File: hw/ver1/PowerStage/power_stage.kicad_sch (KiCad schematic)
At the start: 56 parts, among them J4 Conn_02x12_Odd_Even, J5 Conn_01x02_Socket, Q1 2N7002, SW1 SW_DIP_x03, U3 74HC4051, U4 LTC7871

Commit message: Save this morning's effort
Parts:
- added C23, C28, C29, C30, C31, C32, C33, C34, C35, C36, C37, C38, C39, C40: 2uF, symbol Device:C
- added C24, C25, C26, C27: 220uF, symbol Device:C_Polarized
- added R35, R52: 10k, Resistor_SMD:R_0603_1608Metric, symbol Device:R_US
- added U10: LM1117MP-3.3, Package_TO_SOT_SMD:SOT-223-3_TabPin2, symbol Regulator_Linear:LM1117MP-3.3
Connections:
- net +12P: now also C40.1, U10.3 (VI)
- net +3.3VP: now also C39.1, U10.2 (VO)
- net +5P: now also R35.2
- net GND: now also C23.2, C24.2, C25.2, C26.2, C27.2, C28.2, C29.2, C30.2, C31.2, C32.2, C33.2, C34.2, C35.2, C36.2, C37.2, C38.2, C39.2, C40.2, U10.1 (GND)
- net GNDD: now also R52.2
- net HT: now also C31.1, C32.1, C33.1, C34.1, C35.1, C36.1, C37.1, C38.1
- net VBUS: no longer R25.1
- net Phase1/SNSA+: now reaches U4.17 (SNSA1+)
- net Phase1/SNSD-: now reaches U4.18 (SNS1-)
- net Phase1/SNSD+: now reaches U4.19 (SNSD1+)
- net Phase2/SNSD+: now reaches U4.20 (SNSD2+)
- net Phase2/SNSD-: now reaches U4.21 (SNS2-)
- net Phase2/SNSA+: now reaches U4.22 (SNSA2+)
- net Phase3/SNSA+: now reaches U4.23 (SNSA3+)
- net Phase3/SNSD-: now reaches U4.24 (SNS3-)
- net Phase3/SNSD+: now reaches U4.25 (SNSD3+)
- net Phase1/PWMEN: now reaches U4.28 (PWMEN)
- net Phase1/PWMEN: now also R35.1
- net Phase1/PWM: now reaches U4.29 (PWM1)
- net Phase2/PWM: now reaches U4.31 (PWM2)
- net Phase3/PWM: now reaches U4.32 (PWM3)
- net Phase4/PWM: now reaches U4.33 (PWM4)
- net DisabledPhase5/PWM: now reaches U4.34 (PWM5)
- net DisabledPhase6/PWM: now reaches U4.36 (PWM6)
- net at U4.50 (CLKOUT): now also R52.1
- net Phase4/SNSD+: now reaches U4.56 (SNSD4+)
- net Phase4/SNSD-: now reaches U4.57 (SNS4-)
- net Phase4/SNSA+: now reaches U4.58 (SNSA4+)
- net DisabledPhase5/SNSA+: now reaches U4.59 (SNSA5+)
- net DisabledPhase5/SNSD-: now reaches U4.60 (SNS5-)
- net DisabledPhase5/SNSD+: now reaches U4.61 (SNSD5+)
- net DisabledPhase6/SNSD+: now reaches U4.62 (SNSD6+)
- net DisabledPhase6/SNSD-: now reaches U4.63 (SNS6-)
- net DisabledPhase6/SNSA+: now reaches U4.64 (SNSA6+)
- new net VLOW: C23.1, C24.1, C25.1, C26.1, C27.1, C28.1, C29.1, C30.1, R25.1
- no-connect marks 2 -> 1
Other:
- added sheet DisabledPhase5 (power_stage_n_disabled.kicad_sch)
- added sheet DisabledPhase6 (power_stage_n_disabled.kicad_sch)
- added sheet Phase1 (power_stage_n.kicad_sch)
- added sheet Phase2 (power_stage_n.kicad_sch)
- added sheet Phase3 (power_stage_n.kicad_sch)
- added sheet Phase4 (power_stage_n.kicad_sch)
- note added: "Input Filtering"
- note added: "Output Filtering"
- moved on the sheet: R25, R26, R3, R4, R5, R6

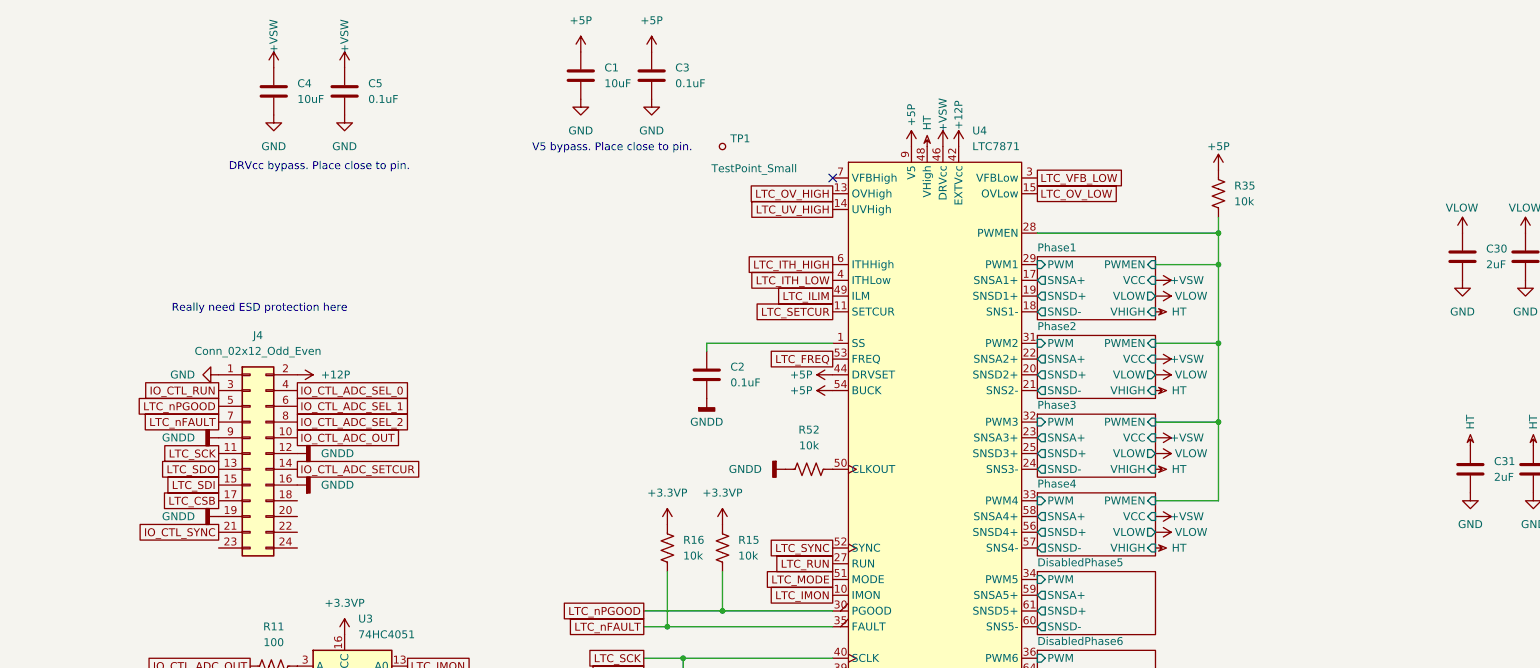
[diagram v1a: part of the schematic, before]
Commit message: Split controller from the power stage. Get a better high level system flow.
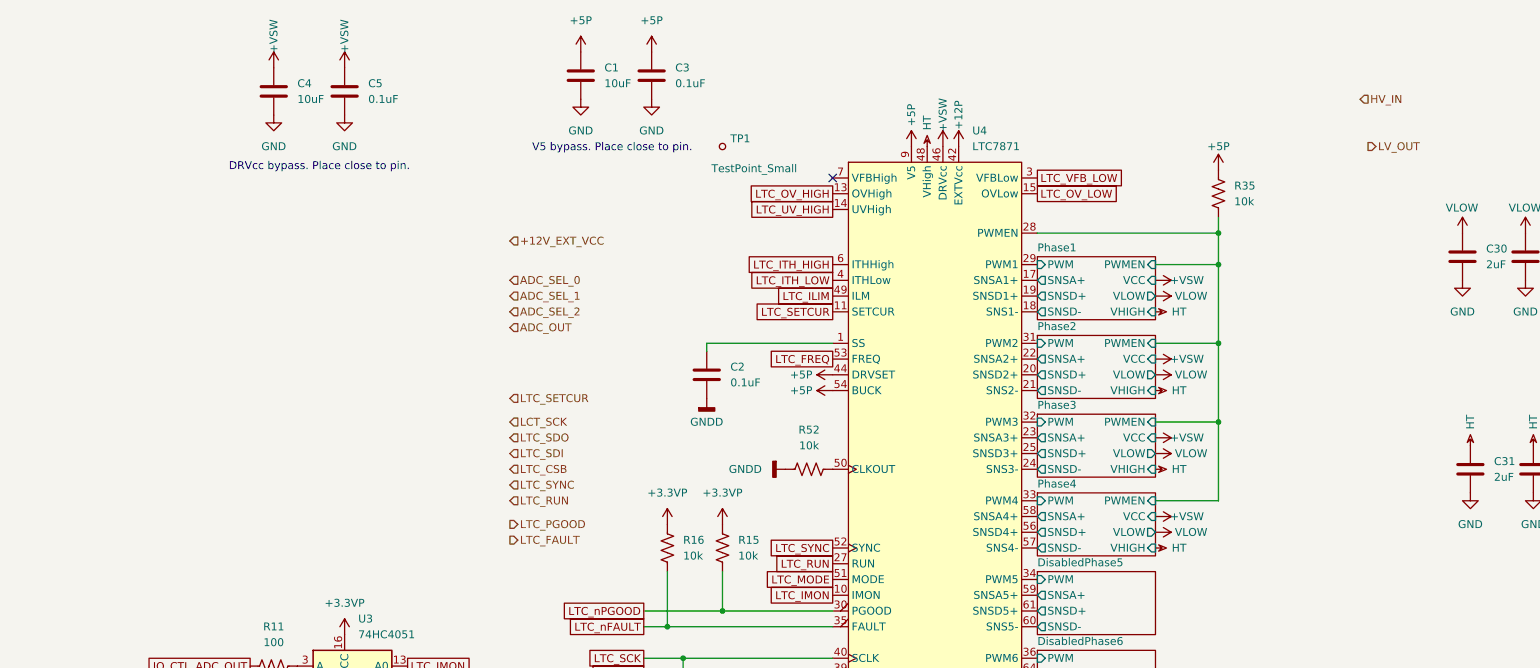
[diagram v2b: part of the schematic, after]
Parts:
- removed J4: Conn_02x12_Odd_Even, symbol Connector_Generic:Conn_02x12_Odd_Even
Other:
- note removed: "Really need ESD protection here"

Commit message: Sync wip
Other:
- note added: "Only enable one at a time. Both GND == floating. NPN PNP? Or MOS?"

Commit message: Save lunchtime work
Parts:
- removed JP2: Jumper_3_Open, Jumper:SolderJumper-3_P1.3mm_Open_RoundedPad1.0x1.5mm_NumberLabels, symbol Jumper:Jumper_3_Open
- removed JP4: Jumper_2_Open, symbol Jumper:Jumper_2_Open
- removed Q1: 2N7002, Package_TO_SOT_SMD:SOT-23, symbol Transistor_FET:2N7002
- added C65: 2uF, symbol Device:C
- added JP3: SolderJumper_2_Bridged, Jumper:SolderJumper-2_P1.3mm_Bridged_RoundedPad1.0x1.5mm, symbol Jumper:SolderJumper_2_Bridged
- added Q1: BSS84, Package_TO_SOT_SMD:SOT-23, symbol Transistor_FET:BSS84
- added Q6, Q7, Q8: BSS138, Package_TO_SOT_SMD:SOT-23, symbol Transistor_FET:BSS138
- added R61, R65: 100, Resistor_SMD:R_0603_1608Metric, symbol Device:R_US
- added R62, R63, R64, R66: 10k, Resistor_SMD:R_0603_1608Metric, symbol Device:R_US
- R27: value 10k -> 22k
- R28: value 10k -> 1k
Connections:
- net +5P: now also Q1.2 (S), R63.2
- net GND: now also C65.2
- net GNDD: now also Q6.2 (S), Q7.2 (S), Q8.2 (S), R62.1, R66.1
- net LTC_MODE: now also Q6.3 (D), R64.2
- net LTC_SETCUR: now also C65.1
- net LTC_SYNC: now also JP3.2 (B)
- net at R7.2, R9.1: now also Q7.1 (G)
- net at R8.1: now also JP3.1 (A), Q7.3 (D)
- net DisabledPhase5/PWM renamed Phase5/PWM
- net DisabledPhase5/SNSA+ renamed Phase5/SNSA+
- net DisabledPhase5/SNSD+ renamed Phase5/SNSD+
- net DisabledPhase5/SNSD- renamed Phase5/SNSD-
- net DisabledPhase6/PWM renamed Phase6/PWM
- net DisabledPhase6/SNSA+ renamed Phase6/SNSA+
- net DisabledPhase6/SNSD+ renamed Phase6/SNSD+
- net DisabledPhase6/SNSD- renamed Phase6/SNSD-
- net IO_CTL_ADC_OUT renamed IO_ADC_OUT
- net IO_CTL_ADC_SEL_0 renamed IO_ADC_SEL_0
- net IO_CTL_ADC_SEL_1 renamed IO_ADC_SEL_1
- net IO_CTL_ADC_SEL_2 renamed IO_ADC_SEL_2
- net IO_CTL_ADC_SETCUR renamed IO_LTC_SETCUR
- net IO_CTL_RUN renamed IO_LTC_RUN
- net IO_CTL_SYNC renamed IO_LTC_SYNC
- net LTC_CSB renamed IO_LTC_CSB
- net LTC_SCK renamed IO_LCT_SCK
- net LTC_SDI renamed IO_LTC_SDI
- net LTC_SDO renamed IO_LTC_SDO
- net LTC_nFAULT renamed IO_LTC_FAULT
- net LTC_nPGOOD renamed IO_LTC_PGOOD
- new net: Q6.1 (G), R61.1, R62.2
- new net: Q8.1 (G), R65.1, R66.2
- new net: Q1.1 (G), Q8.3 (D), R63.1
- new net: Q1.3 (D), R64.1
- new net IO_LTC_CCM: R61.2
- new net IO_LTC_DCCM: R65.2
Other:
- removed sheet DisabledPhase5
- removed sheet DisabledPhase6
- added sheet Phase5 (power_stage_n.kicad_sch)
- added sheet Phase6 (power_stage_n.kicad_sch)
- note added: "CCM=0, DCM=0: Burst Mode CCM=0, DCM=1: Discontinuous Conduction Mode CCM=1, DCM=0: Forced Continuous Conduction Mode CCM=1, DCM=1: Forced Continuous Conduction Mode"
- note added: "TODO: This isn't designed yet!"
- note removed: "+5V == Discontinuous Mode GND == Forced Continuous Mode FLT == Burst Mode"
- note removed: "From ltc7871.ipynb, 1kW, 4phase output DCR Sense 30mV"
- note removed: "Only enable one at a time. Both GND == floating. NPN PNP? Or MOS?"
- moved on the sheet: R24

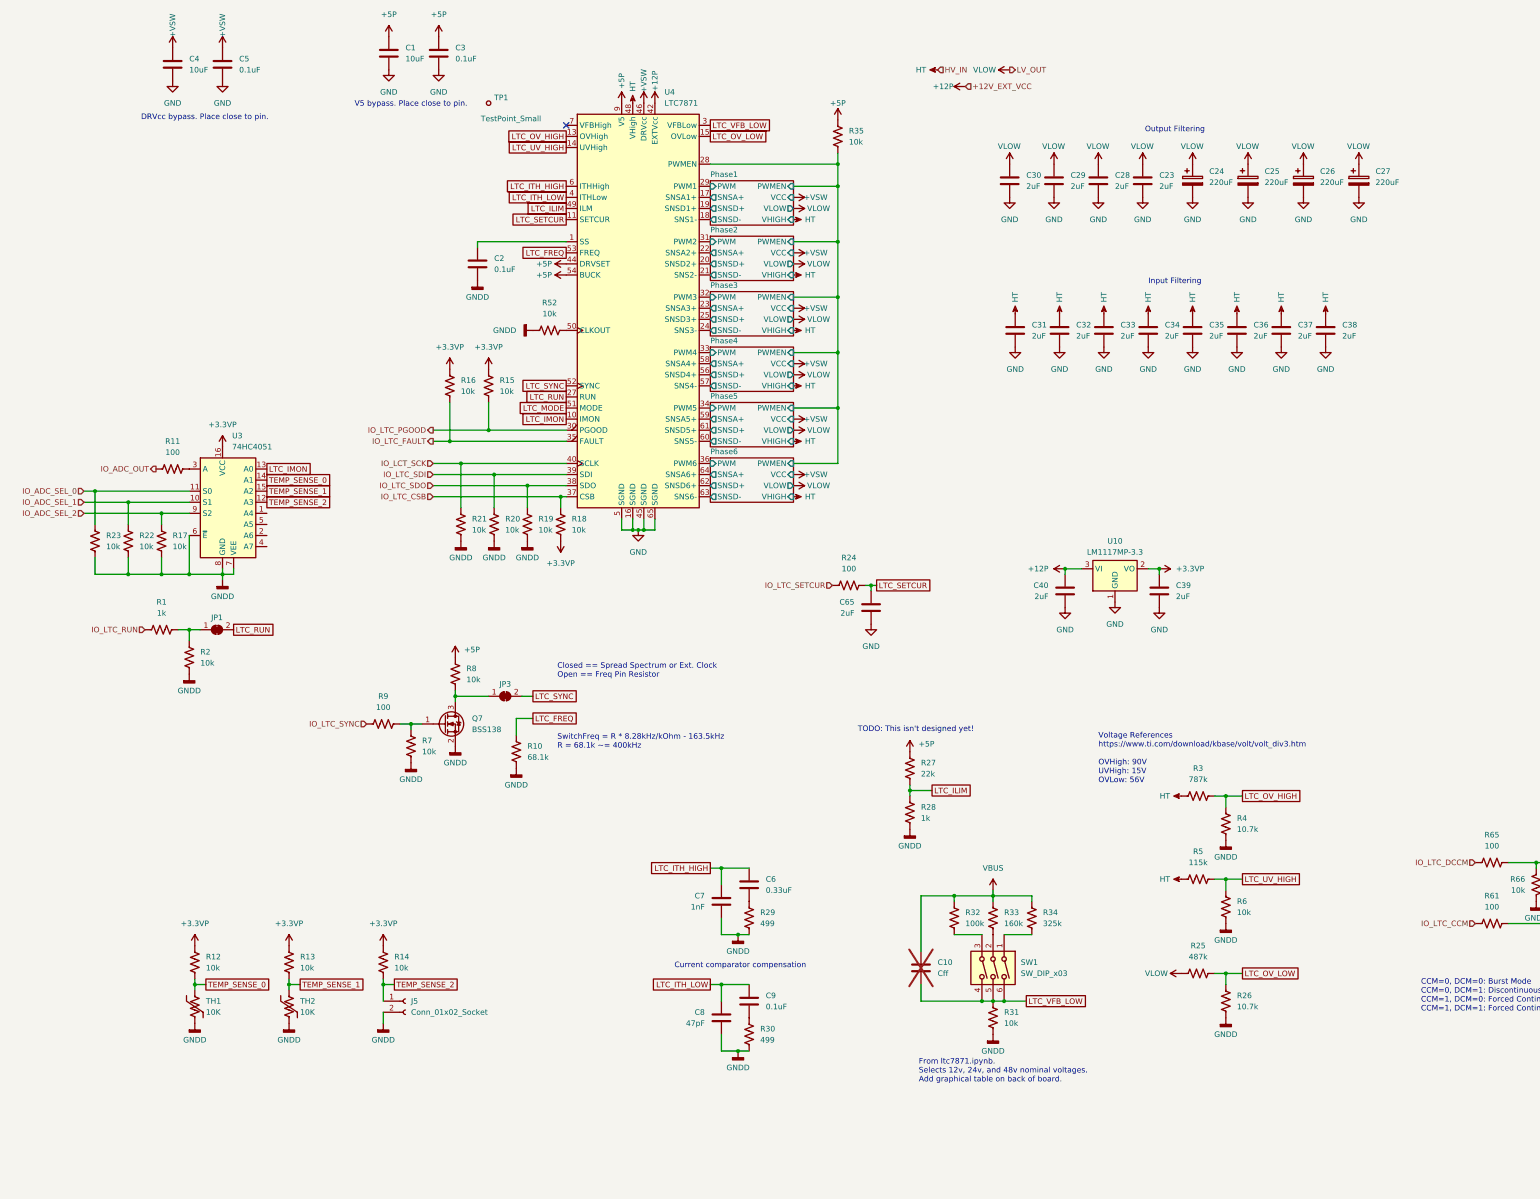
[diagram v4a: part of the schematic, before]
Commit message: Add component part numbers for ordering. Resolve footprints.
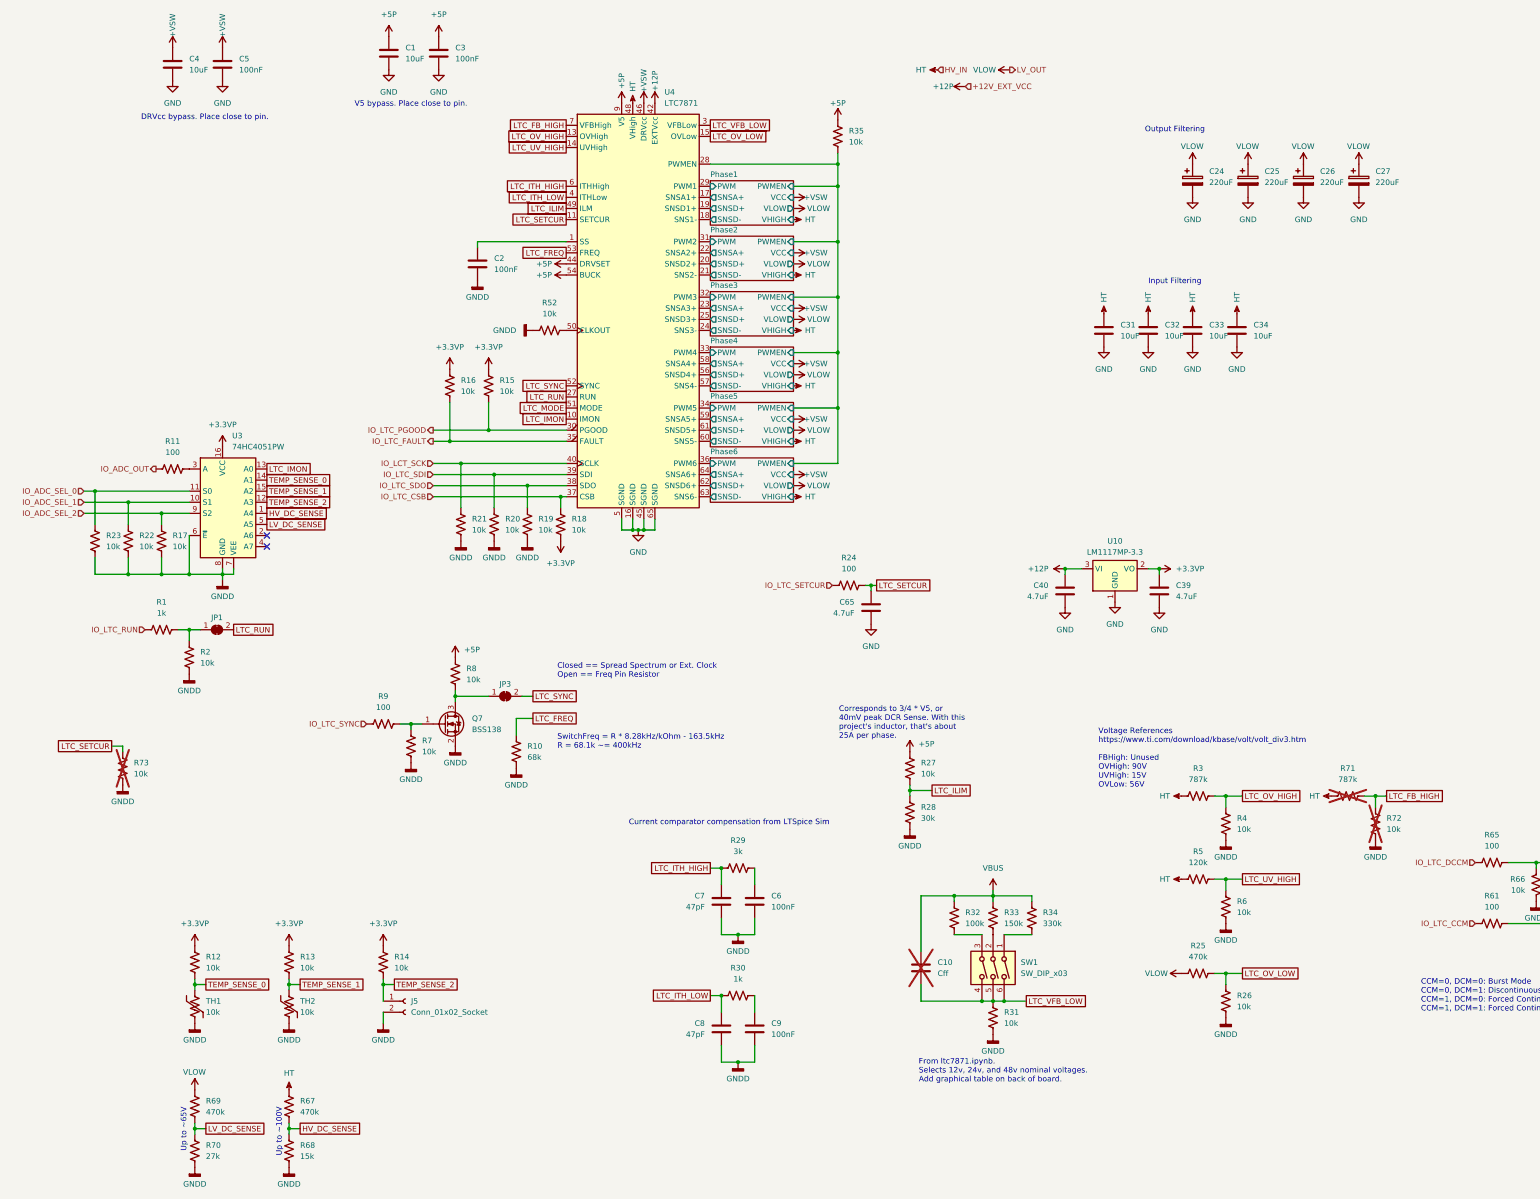
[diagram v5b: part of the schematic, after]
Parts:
- removed C23, C28, C29, C30, C35, C36, C37, C38: 2uF, symbol Device:C
- removed TP1: TestPoint_Small, symbol Connector:TestPoint_Small
- added R67, R69: 470k, Resistor_SMD:R_0603_1608Metric, symbol Device:R_US
- added R68: 15k, Resistor_SMD:R_0603_1608Metric, symbol Device:R_US
- added R70: 27k, Resistor_SMD:R_0603_1608Metric, symbol Device:R_US
- added R71: 787k, Resistor_SMD:R_0603_1608Metric_Pad0.98x0.95mm_HandSolder, symbol Device:R_US
- added R72, R73: 10k, Resistor_SMD:R_0603_1608Metric, symbol Device:R_US
- C1, C4: footprint (none) -> Capacitor_SMD:C_0603_1608Metric; Digikey (none) -> N/A; LCSC (none) -> C96446
- C10: footprint (none) -> Capacitor_SMD:C_0603_1608Metric_Pad1.08x0.95mm_HandSolder; Digikey (none) -> N/A; LCSC (none) -> N/A
- C2, C3, C5, C9: value 0.1uF -> 100nF; footprint (none) -> Capacitor_SMD:C_0603_1608Metric; Digikey (none) -> N/A; LCSC (none) -> C14663
- C24, C25, C26, C27: footprint (none) -> Capacitor_THT:CP_Radial_D10.0mm_P5.00mm; Digikey (none) -> 1189-3789-1-ND; LCSC (none) -> N/A
- C31, C32, C33, C34: value 2uF -> 10uF; footprint (none) -> Capacitor_SMD:C_1210_3225Metric_Pad1.33x2.70mm_HandSolder; Digikey (none) -> 490-16266-1-ND
- C39, C40, C65: value 2uF -> 4.7uF; footprint (none) -> Capacitor_SMD:C_0603_1608Metric; Digikey (none) -> N/A; LCSC (none) -> C19666
- C6: value 0.33uF -> 100nF; footprint (none) -> Capacitor_SMD:C_0603_1608Metric; Digikey (none) -> N/A; LCSC (none) -> C14663
- C7: value 1nF -> 47pF; footprint (none) -> Capacitor_SMD:C_0603_1608Metric; Digikey (none) -> N/A; LCSC (none) -> C1671
- C8: footprint (none) -> Capacitor_SMD:C_0603_1608Metric; Digikey (none) -> N/A; LCSC (none) -> C1671
- J5: footprint (none) -> Connector_PinSocket_2.54mm:PinSocket_1x02_P2.54mm_Vertical; Digikey (none) -> N/A; LCSC (none) -> N/A
- JP1, JP3: Digikey (none) -> N/A; LCSC (none) -> N/A
- Q1: Digikey (none) -> 5272-BSS84CT-ND; LCSC (none) -> N/A
- Q6, Q7, Q8: Digikey (none) -> 5272-BSS138CT-ND; LCSC (none) -> N/A
- R1: Digikey (none) -> N/A; LCSC (none) -> C21190
- R10: value 68.1k -> 68k; Digikey (none) -> N/A; LCSC (none) -> C23231
- R11, R24, R61, R65, R9: Digikey (none) -> N/A; LCSC (none) -> C22775
- R12, R13, R14, R15, R16, R17, R18, R19, R2, R20, R21, R22, R23, R31, R35, R52, R6, R62, R63, R64, R66, R7, R8: Digikey (none) -> N/A; LCSC (none) -> C25804
- R25: value 487k -> 470k; Digikey (none) -> N/A; LCSC (none) -> C23178
- R26, R4: value 10.7k -> 10k; Digikey (none) -> N/A; LCSC (none) -> C25804
- R27: value 22k -> 10k; Digikey (none) -> N/A; LCSC (none) -> C25804
- R28: value 1k -> 30k; Digikey (none) -> N/A; LCSC (none) -> C22984
- R29: value 499 -> 3k; Digikey (none) -> N/A; LCSC (none) -> C4211
- R3: footprint Resistor_SMD:R_0603_1608Metric -> Resistor_SMD:R_0603_1608Metric_Pad0.98x0.95mm_HandSolder; Digikey (none) -> P787KHCT-ND; LCSC (none) -> N/A
- R30: value 499 -> 1k; Digikey (none) -> N/A; LCSC (none) -> C21190
- R32: Digikey (none) -> N/A; LCSC (none) -> C25803
- R33: value 160k -> 150k; Digikey (none) -> N/A; LCSC (none) -> C22807
- R34: value 325k -> 330k; Digikey (none) -> N/A; LCSC (none) -> C23137
- R5: value 115k -> 120k; Digikey (none) -> N/A; LCSC (none) -> C25808
- SW1: footprint (none) -> Button_Switch_SMD:SW_DIP_SPSTx03_Slide_6.7x9.18mm_W6.73mm_P2.54mm_LowProfile_JPin; Digikey (none) -> CT2193LPST-ND; LCSC (none) -> N/A
- TH1, TH2: value 10K -> 10k; footprint (none) -> Resistor_SMD:R_0402_1005Metric_Pad0.72x0.64mm_HandSolder; Digikey (none) -> 445-2550-1-ND; LCSC (none) -> N/A
- U10: Digikey (none) -> 488-LM1117MPX-33NOPBCT-ND; LCSC (none) -> C23984
- U3: value 74HC4051 -> 74HC4051PW; footprint (none) -> Package_SO:TSSOP-14_4.4x5mm_P0.65mm; Digikey (none) -> 1727-3064-1-ND; LCSC (none) -> N/A
- U4: Digikey (none) -> 505-LTC7871ELWE#PBF-ND; LCSC (none) -> C690288
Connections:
- net GNDD: now also C6.2, C9.2, R68.1, R70.1, R72.1, R73.1; no longer R29.1, R30.1
- net HT: now also R67.2, R71.1
- net LTC_ITH_HIGH: now also R29.2; no longer C6.1
- net LTC_ITH_LOW: now also R30.2; no longer C9.1
- net LTC_SETCUR: now also R73.2
- net VLOW: now also R69.2
- net HV_DC_SENSE: now reaches U3.1 (A4)
- net HV_DC_SENSE: now also R67.1, R68.2
- net LV_DC_SENSE: now reaches U3.5 (A5)
- net LV_DC_SENSE: now also R69.1, R70.2
- net LTC_FB_HIGH: now reaches U4.7 (VFBHigh)
- net LTC_FB_HIGH: now also R71.2, R72.2
- new net: C6.1, R29.1
- new net: C9.1, R30.1
- no-connect marks 1 -> 2
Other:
- note added: "Corresponds to 3/4 * V5, or 40mV peak DCR Sense. With this project's inductor, that's about 25A per phase."
- note added: "Current comparator compensation from LTSpice Sim"
- note added: "Up to ~100V"
- note added: "Up to ~65V"
- note added: "Voltage References https://www.ti.com/download/kbase/volt/volt_div3.htm FBHigh: Unused OVHigh: 90V UVHigh: 15V OVLow: 56V"
- note removed: "Current comparator compensation"
- note removed: "TODO: This isn't designed yet!"
- note removed: "Voltage References https://www.ti.com/download/kbase/volt/volt_div3.htm OVHigh: 90V UVHigh: 15V OVLow: 56V"
- moved on the sheet: C34, C8, C9, R29, R30

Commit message: Sync some start to the PCB design
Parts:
- C12: renamed from C7; footprint Capacitor_SMD:C_0603_1608Metric -> Capacitor_SMD:C_0603_1608Metric
- C13: renamed from C8; footprint Capacitor_SMD:C_0603_1608Metric -> Capacitor_SMD:C_0603_1608Metric
- renumbered C3 to C10, C2 to C11, C6 to C14, C9 to C15, C65 to C16, C10 to C17, C40 to C18, C31 to C19, C32 to C20, C39 to C21, C24 to C22, C33 to C23, C34 to C24, C4 to C7, C5 to C8, C1 to C9, J5 to J7, JP3 to JP2, Q7 to Q3, Q8 to Q4, Q1 to Q5, R1 to R10, R2 to R12, R12 to R13, R69 to R14, R70 to R15, R13 to R16, R67 to R17, R68 to R18, R9 to R19, R14 to R20, R7 to R21, R16 to R22, R8 to R23, R21 to R24, R15 to R25, R20 to R26, R10 to R27, R19 to R28, R52 to R29, R18 to R30, R29 to R31, R30 to R32, R35 to R33, R24 to R34, R27 to R35, R28 to R36, R32 to R37, R33 to R38, R31 to R39, R34 to R40, R3 to R41, R5 to R42, R25 to R43, R4 to R44, R6 to R45, R26 to R46, R71 to R47, R72 to R48, R65 to R49, R61 to R50, R66 to R51, R63 to R52, R62 to R53, R64 to R54, R23 to R6, R73 to R7, R22 to R8, R17 to R9, U3 to U2, U4 to U3, U10 to U4
